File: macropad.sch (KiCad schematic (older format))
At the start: 24 parts, among them SW1 SW_Push, U1 ATmega32U4-AU, Y1 16MHz

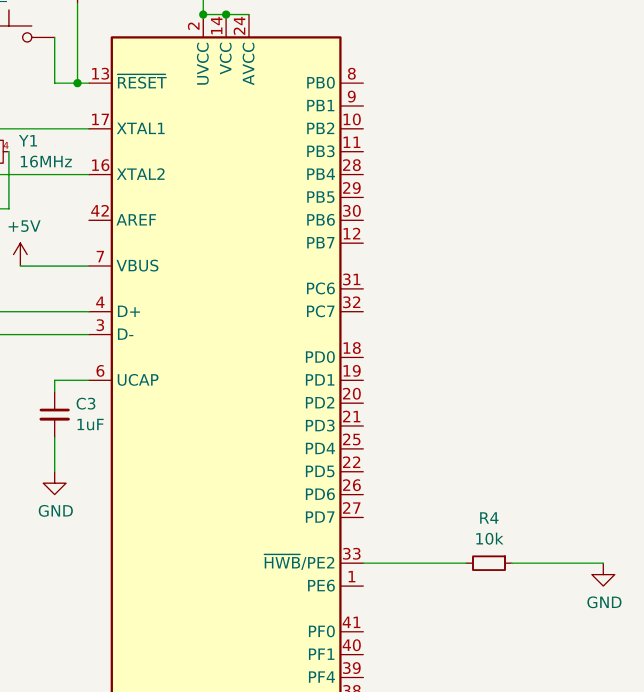
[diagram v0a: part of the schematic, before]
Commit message: Completed macropad
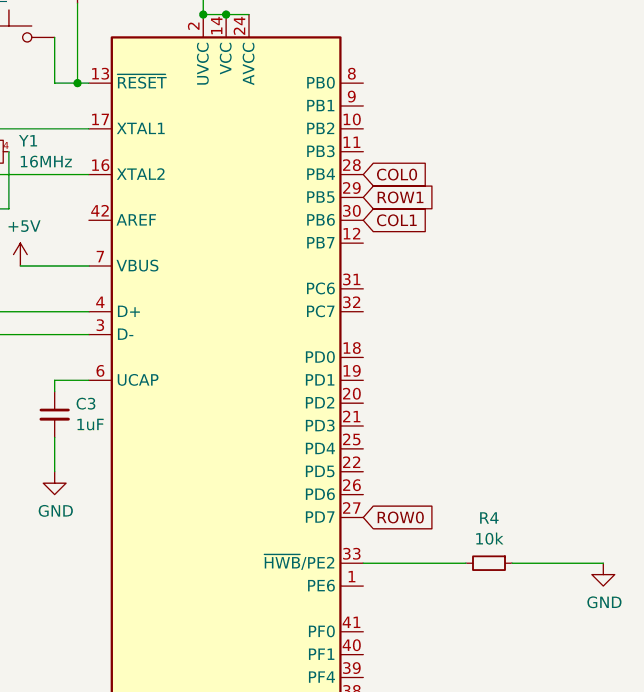
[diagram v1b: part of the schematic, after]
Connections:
- net COL0: now also U1.28 (PB4)
- net COL1: now also U1.30 (PB6)
- net ROW0: now also U1.27 (PD7)
- net ROW1: now also U1.29 (PB5)
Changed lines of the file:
@@
 Text GLabel 3200 3150 0    50   Input ~ 0
 ROW1
+Text GLabel 9600 3600 2    50   Input ~ 0
+ROW0
+Text GLabel 9600 2100 2    50   Input ~ 0
+COL0
+Text GLabel 9600 2300 2    50   Input ~ 0
+COL1
+Text GLabel 9600 2200 2    50   Input ~ 0
+ROW1
 $EndSCHEMATC
